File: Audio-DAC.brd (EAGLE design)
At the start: 99 x 99 mm, 201 parts, among them CON1 USB-5075BR-04-WH, CON2 VOL_CON, CON3 SWD_CON, IC1 3.3V 200mA, IC10 15V, IC11 -15V, IC12 3.3V, IC13 LPC1114FDH28, IC14 10V, IC15 5V, IC16 5V, IC17 3.3V, IC18 TC7WH74FU, IC19 AK4495EQ, IC2 AT32UC3A3256, IC20 TC7WU04FU, IC21 10V, IC22 -10V, IC23 OP275, IC3 SI8420, IC4 SI8420, IC5 SI8420, IC6 SI8420, IC9 7805, Q1 NPN2SC3422, Q2 PNP2SA1359, Q3 NPN2SC3422, Q4 PNP2SA1359, Q5 NPN2SC3325, Q6 NPN2SC3325, SW1 EA2, SW2 EA2, X1 12MHz, X2 24.576MHz, X3 22.5792MHz

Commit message: 発注
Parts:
- removed JP1: SPK, pinhead:1X04
- removed JP2: HP, pinhead:1X04
- added R15: 100, my_rcl:1608-J
- added R16: DNP, my_rcl:1608-J
- added TP25: GND, my_connector:TESTPIN
- added TP26: +3V3D, my_connector:TESTPIN
- added TP27, TP31: GND_L, my_connector:TESTPIN-BIG
- added TP28: SPK_L, my_connector:TESTPIN-BIG
- added TP29: SPK_R, my_connector:TESTPIN-BIG
- added TP30, TP34: GND_R, my_connector:TESTPIN-BIG
- added TP32: HP_L, my_connector:TESTPIN-BIG
- added TP33: HP_R, my_connector:TESTPIN-BIG
- C47, C48, C52, C54: value 0.22u -> 0.1u
- C49, C50, C55, C56: value DNP -> 0.1u
- C63, C64, C65, C66: value 2000p -> 10n
- CON1: value USB-5075BR-04-WH -> USB-B
- CON2: value VOL_CON -> VOLUEME
- CON3: value SWD_CON -> SWD
- D7, D8: value SBD-1A -> SBD; device my_rcl:TUMD2M -> my_rcl:SOD123
- FB1, FB2, FB3, FB4: value FB-1608 -> FB; device my_rcl:1608 -> my_rcl:1608-J
- IC1: value 3.3V 200mA -> 3.3V
- IC10: value 15V -> +15V
- IC13: value LPC1114FDH28 -> LPC1114
- IC14, IC21: value 10V -> +10V
- IC15, IC16: value 5V -> +5V
- IC17: value 3.3V -> +3.3V
- Q5, Q6: value NPN2SC3325 -> NPN
- R32, R33, R34, R35, R36: device my_rcl:1608 -> my_rcl:1608-J
- R37, R38, R39, R40: value 1k -> 2k
- R41, R42, R43, R44: value 2k -> 4k
- R45, R46, R47, R48: value 1k -> 150
- TP10: value TEST_11 -> GND
- TP11: value TEST_10 -> SDA
- TP13: value GND -> TEST_10
- TP14: value +3V3 -> TEST_14
- TP15, TP18: value SP_SW -> SP
- TP16: value HP_SW -> HP
- TP17: value GND -> +12V
- TP19: value HP_SW -> GND
- TP20: value +12V -> HP
- TP23: value SDA -> TEST_11
- TP5: value VIN+ -> V+
- TP8: value VIN- -> V-
- TP9: value TEST_12 -> +3V3
- moved TP17 69.6 mm to (91.4, 91.4)
- moved TP21 69.0 mm to (36.8, 48.3)
- moved TP23 8.03 mm to (45.7, 26.7)
- moved TP6 7.62 mm to (73.7, 5.08)
- moved TP20 7.41 mm to (94.0, 88.9)
- moved DR3 6.35 mm to (89.5, 3.17)
- moved DR4 6.35 mm to (89.5, 95.9)
- moved TP11 5.68 mm to (38.1, 29.2)
- moved TP14 5.08 mm to (45.7, 24.1)
- moved TP9 5.08 mm to (45.7, 29.2)
- moved TP7 5.08 mm to (78.7, 5.08)
- moved FB2 4.05 mm to (9.84, 55.2), turned to 0 degrees
- moved TP10 3.59 mm to (43.2, 29.2)
- moved DR2 3.17 mm to (6.35, 95.9)
- moved D8 2.73 mm to (93.0, 77.8)
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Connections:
- removed net N$37: IC13.14, TP9.1
- removed net N$53: IC13.10, TP11.1
- new net N$15: C1.1, IC1.4
- new net N$16: D7.1, Q5.3, SW1.1
- new net N$19: IC13.14, TP14.1
- net +12V: now also D7.2, D8.2, SW1.10, TP17.1; no longer D7.K, D8.K, SW1.1, TP20.1
- net +3V3: now also TP9.1; no longer TP14.1
- net +3V3D: now also IC1.5, TP26.1; no longer IC1.4
- net DAC_DVDD: now also IC19.44; no longer IC19.43
- net DAC_LRCLK: now also R15.1
- net DGND: now also TP25.1
- net EN_+3V3D: now also IC1.3, R16.1; no longer IC1.1
- net GND: now also IC19.43, IC9.2, TP10.1, TP19.1, TP27.1, TP30.1, TP31.1, TP34.1; no longer IC19.44, IC9.3, JP1.1, JP1.4, JP2.1, JP2.4, TP13.1, TP17.1
- net HP_L: now also TP32.1; no longer JP2.2
- net HP_R: now also TP33.1; no longer JP2.3
- net HP_SW: now also TP20.1; no longer TP19.1
- net I2C_SDA: now also TP11.1; no longer TP23.1
- net N$18: now also IC13.10, TP13.1; no longer C1.1, IC1.3
- net N$36: now also IC13.11, TP23.1; no longer D7.A, Q5.3, SW1.10
- net N$38: now also IC13.2, R15.2; no longer IC13.11, TP10.1
- net N$49: now also D8.1; no longer D8.A
- net N$51: now also IC9.3; no longer IC9.2
- net SPK_L: now also TP28.1; no longer JP1.2
- net SPK_R: now also TP29.1; no longer JP1.3
- net USB_VBUS: now also IC1.1, R16.2; no longer IC1.5
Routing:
- net N$19: track 0.00 -> 20.0 mm, vias 0 -> 1
- net N$37: track 19.3 -> 0.00 mm, vias 1 -> 0
- net N$53: track 16.5 -> 0.00 mm
- net N$16: track 0.00 -> 15.7 mm
- net N$18: track 1.76 -> 16.9 mm
- net N$38: track 17.2 -> 10.2 mm
- net GND: track 138.2 -> 145.2 mm
- net V-: track 117.4 -> 110.6 mm, vias 5 -> 3
- net N$49: track 14.5 -> 9.35 mm
- net N$36: track 21.3 -> 17.9 mm
- net N$10: track 6.36 -> 3.42 mm
- net USB_VBUS: track 35.1 -> 38.0 mm
- net +3V3: track 110.3 -> 112.6 mm
- net DAC_DVDD: track 7.88 -> 5.68 mm
- net V+: track 148.1 -> 146.2 mm
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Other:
- board size 99 x 99 mm -> 97 x 99 mm
- board text added: "Audio DAC v6.1"
- board text removed: "Audio DAC v6"

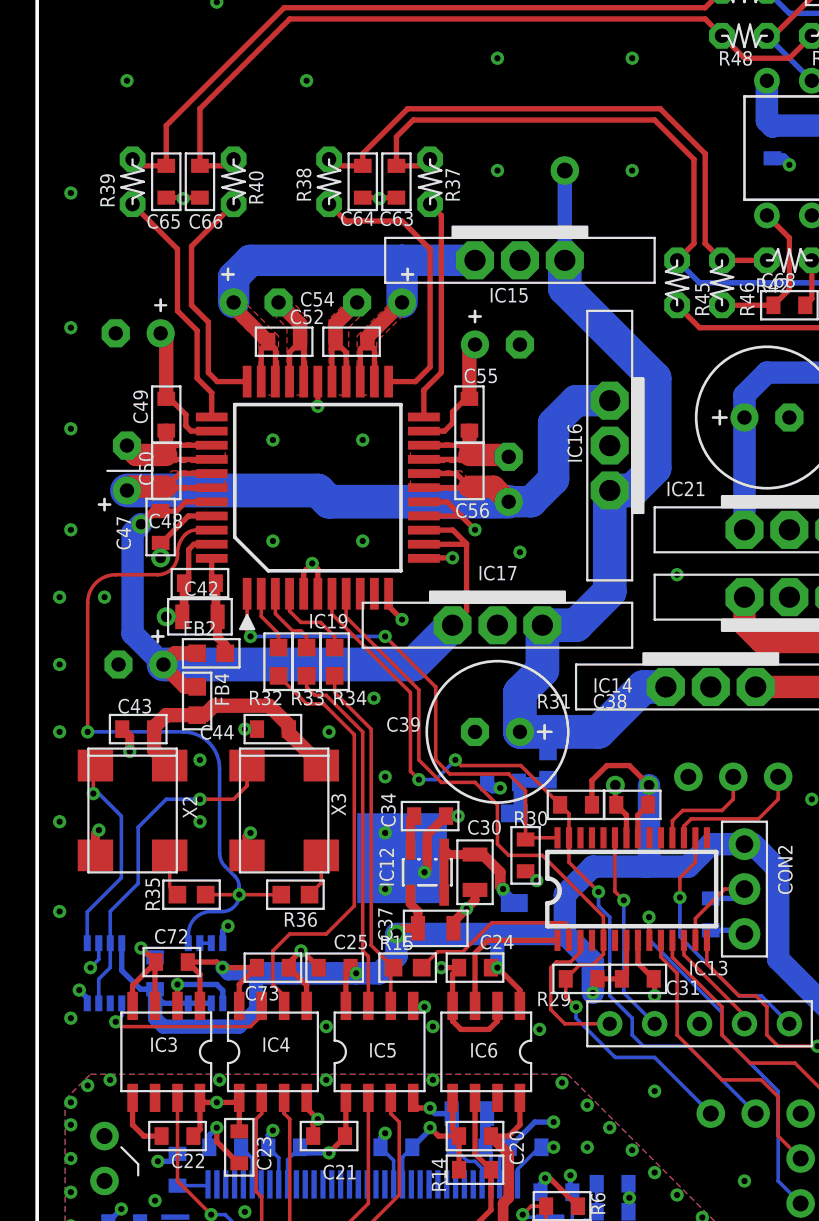
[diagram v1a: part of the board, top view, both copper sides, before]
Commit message: Change to AK4493
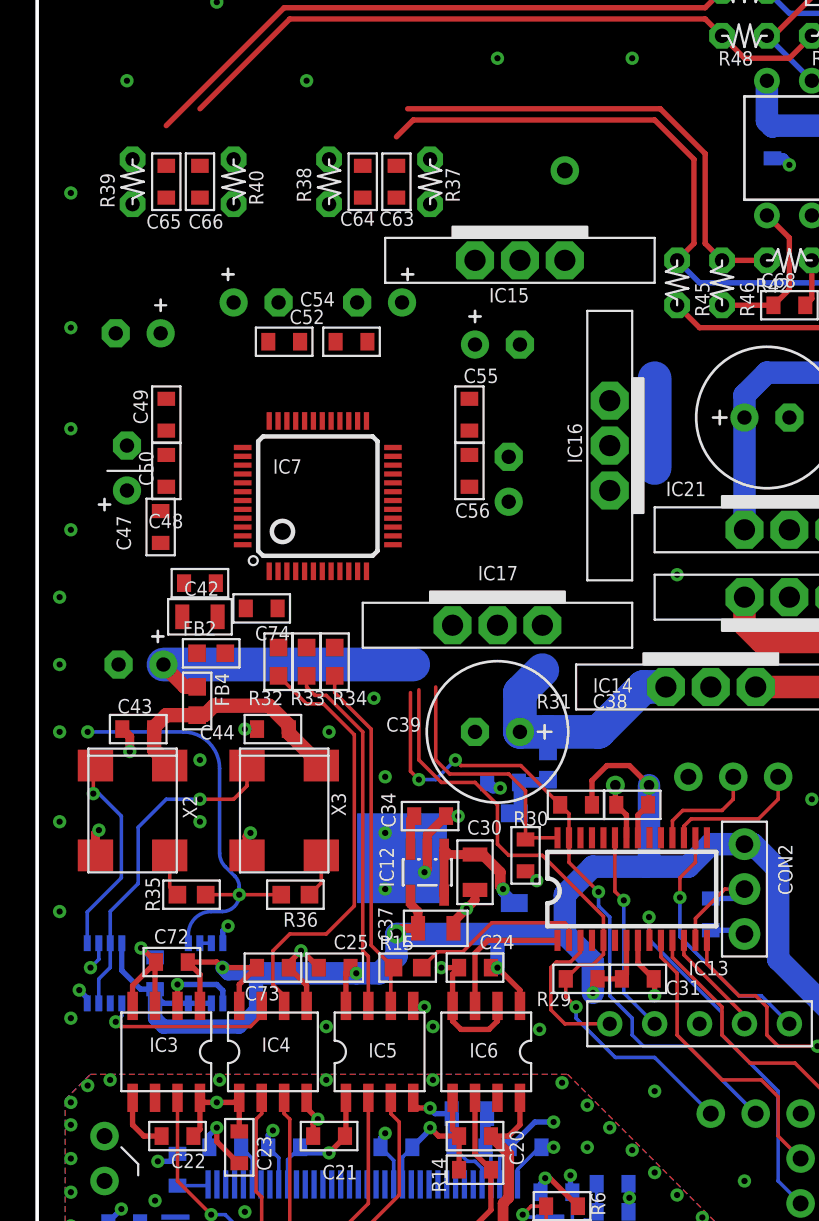
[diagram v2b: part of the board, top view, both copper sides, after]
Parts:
- removed IC19: AK4495EQ, my_ic:LQFP44
- added C74: 1u, my_rcl:1608
- added IC7: AK4493EQ, my_ic:LQFP48
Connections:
- new net N$37: C74.1, IC7.1
- net DAC_AVDD: now also IC7.14, IC7.15, IC7.16, IC7.44; no longer IC19.13, IC19.14, IC19.40
- net DAC_DVDD: now also IC7.48; no longer IC19.44
- net DAC_LN: now also IC7.35; no longer IC19.33
- net DAC_LP: now also IC7.36; no longer IC19.34
- net DAC_MCLK: now also IC7.46; no longer IC19.42
- net DAC_PDN: now also IC7.2; no longer IC19.1
- net DAC_RN: now also IC7.26; no longer IC19.23
- net DAC_RP: now also IC7.25; no longer IC19.22
- net DAC_VCC: now also IC7.27, IC7.28, IC7.33, IC7.34; no longer IC19.24, IC19.25, IC19.31, IC19.32
- net DAC_VREF: now also IC7.19, IC7.20, IC7.41, IC7.42; no longer IC19.17, IC19.18, IC19.38, IC19.39
- net GND: now also C74.2, IC7.12, IC7.13, IC7.17, IC7.18, IC7.21, IC7.22, IC7.29, IC7.30, IC7.31, IC7.32, IC7.39, IC7.40, IC7.45, IC7.47, IC7.6, IC7.7; no longer IC19.11, IC19.12, IC19.15, IC19.16, IC19.19, IC19.20, IC19.26, IC19.27, IC19.28, IC19.29, IC19.30, IC19.36, IC19.37, IC19.41, IC19.43, IC19.5, IC19.6
- net I2C_SCL: now also IC7.8; no longer IC19.7
- net I2C_SDA: now also IC7.9; no longer IC19.8
- net N$41: now also IC7.3; no longer IC19.2
- net N$42: now also IC7.5; no longer IC19.4
- net N$43: now also IC7.4; no longer IC19.3
- net VCOM_L: now also IC7.38; no longer IC19.35
- net VCOM_R: now also IC7.23; no longer IC19.21
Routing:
- net GND: track 145.2 -> 82.9 mm, vias 95 -> 78
- net DAC_VREF: track 47.6 -> 0.00 mm
- net DAC_VCC: track 33.6 -> 0.00 mm
- net +12V: track 87.1 -> 57.3 mm
- net DAC_AVDD: track 45.4 -> 16.6 mm, vias 1 -> 0
- net DAC_MCLK: track 40.7 -> 24.4 mm
- net DAC_RN: track 16.1 -> 0.00 mm
- net DAC_PDN: track 28.7 -> 14.5 mm, vias 2 -> 0
- net DAC_LP: track 13.9 -> 0.00 mm
- net DAC_LN: track 13.3 -> 0.00 mm
- net DAC_RP: track 12.7 -> 0.00 mm
- net VCOM_L: track 7.54 -> 0.00 mm
- net I2C_SCL: track 45.6 -> 38.2 mm
- net I2C_SDA: track 43.7 -> 36.5 mm
- net VCOM_R: track 6.90 -> 0.00 mm
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- removed copper zone on layer 1, net DAC_VCC
- removed copper zone on layer 1, net DAC_VREF
- removed copper zone on layer 1, net GND

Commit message: 大体できた
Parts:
- removed C71: 10u, my_rcl:2012
- removed TP21: GND, my_connector:TESTPIN
- removed TP22: +12V, my_connector:TESTPIN
- TP15: value SP -> +12V
- TP16: value HP -> +12V
- TP17: value +12V -> SW_SP
- TP18: value SP -> SW_HP
- TP19: value GND -> SW_HP
- TP20: value HP -> SW_SP
- moved R59 69.0 mm to (36.8, 47.6), turned to 270 degrees
- moved R60 66.4 mm to (38.7, 47.6), turned to 90 degrees
- moved R57 66.3 mm to (36.8, 47.6), flipped to the bottom, turned to 270 degrees
- moved R58 64.8 mm to (38.7, 47.6), flipped to the bottom
- moved TP20 64.3 mm to (46.4, 45.7)
- moved TP18 60.8 mm to (46.4, 48.3)
- moved Q6 60.6 mm to (43.5, 48.3), turned to 0 degrees
- moved Q5 60.2 mm to (41.9, 47.6), flipped to the bottom, turned to 90 degrees
- moved D8 59.7 mm to (40.6, 49.2), turned to 90 degrees
- moved D7 58.3 mm to (39.7, 50.8), flipped to the bottom
- moved TP16 42.3 mm to (76.2, 73.0)
- moved Q4 29.0 mm to (88.9, 91.8), turned to 0 degrees
- moved Q3 29.0 mm to (78.7, 91.8), turned to 0 degrees
- moved D5 27.2 mm to (80.0, 88.6), turned to 180 degrees
- moved D6 27.2 mm to (90.2, 88.6), turned to 0 degrees
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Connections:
- removed net HP_SW: IC13.17, R59.2, TP16.1, TP20.1
- removed net N$16: D7.1, Q5.3, SW1.1
- removed net N$49: D8.1, Q6.3, SW2.1
- removed net SP_SW: IC13.18, R57.2, TP15.1, TP18.1
- new net EN_HP: IC13.17, R59.2
- new net EN_SP: IC13.18, R57.2
- new net SW_HP: D8.1, Q6.3, SW2.1, TP18.1, TP19.1
- new net SW_SP: D7.1, Q5.3, SW1.1, TP17.1, TP20.1
- net +12V: now also TP15.1, TP16.1; no longer C71.1, TP17.1, TP22.1
- net GND: no longer C71.2, TP19.1, TP21.1
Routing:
- net DAC_VREF: track 0.00 -> 51.3 mm
- net DAC_VCC: track 0.00 -> 36.8 mm
- net DAC_AVDD: track 16.6 -> 51.4 mm
- net GND: track 82.9 -> 115.8 mm, vias 78 -> 70
- net V-: track 110.6 -> 142.1 mm, vias 3 -> 0
- net +12V: track 57.3 -> 85.7 mm, vias 1 -> 0
- net N$27: track 24.7 -> 52.0 mm, vias 0 -> 1
- net DAC_RN: track 0.00 -> 20.4 mm
- net N$46: track 35.5 -> 16.4 mm
- net DAC_LP: track 0.00 -> 18.4 mm
- net DAC_RP: track 0.00 -> 17.3 mm
- net DAC_LN: track 0.00 -> 17.1 mm
- net N$47: track 26.8 -> 11.1 mm
- net N$16: track 15.7 -> 0.00 mm
- net DAC_MCLK: track 24.4 -> 39.2 mm
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- removed copper zone on layer 16, net GND
- removed copper zone on layer 1, net V+
- removed copper zone on layer 1, net V-
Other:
- board text added: "Audio DAC v7"
- board text removed: "Audio DAC v6.1"

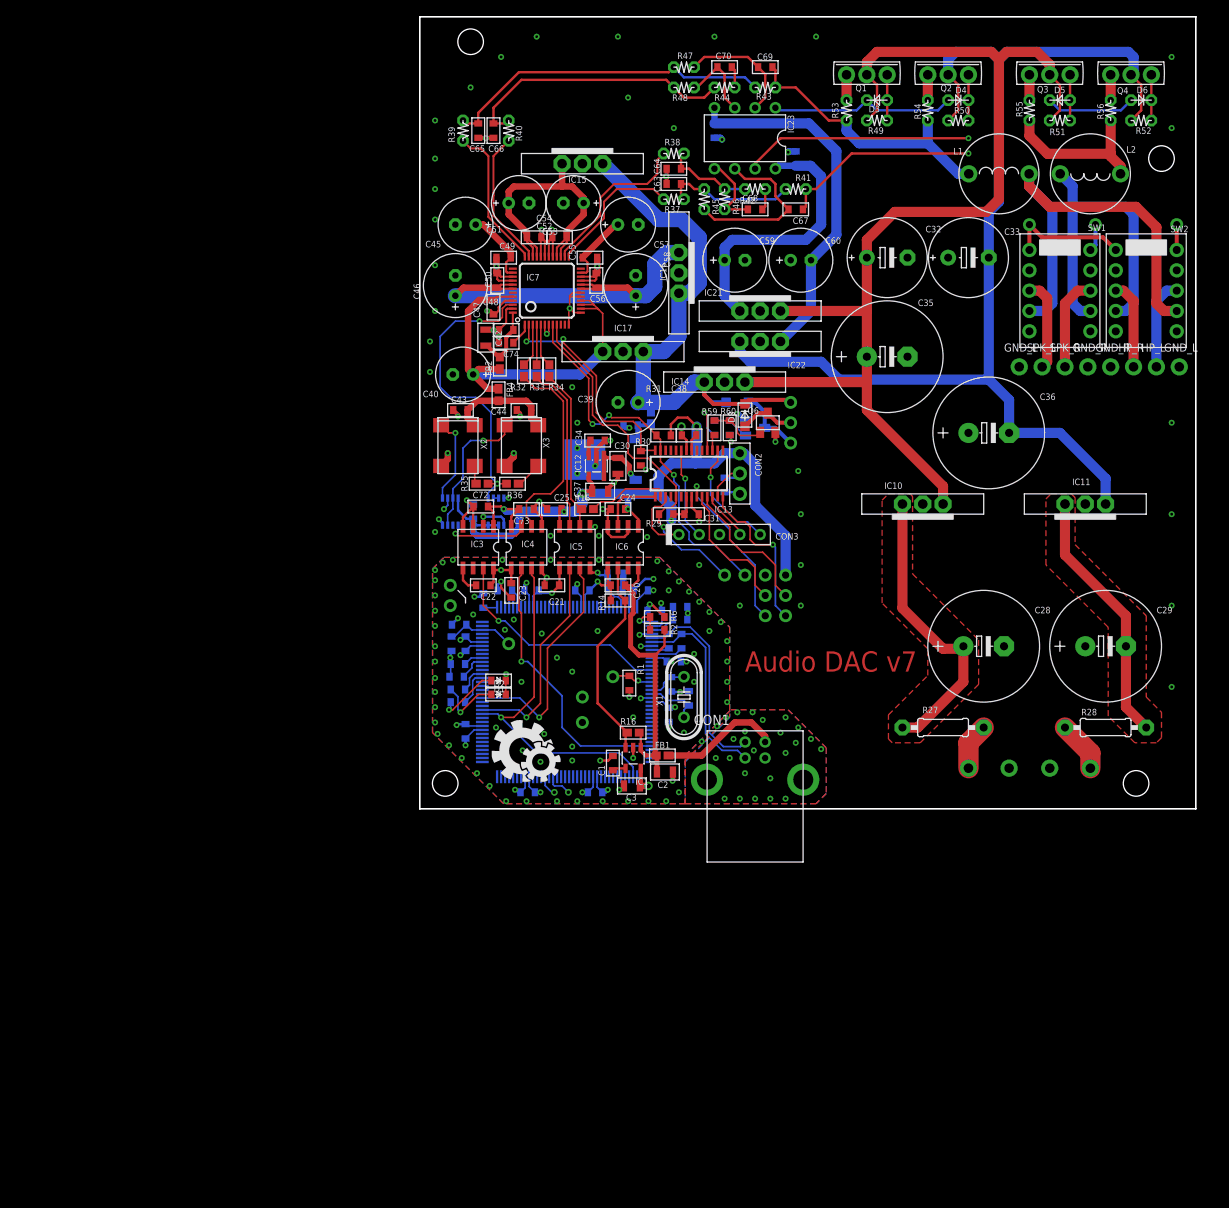
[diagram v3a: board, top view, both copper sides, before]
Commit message: シルク調整
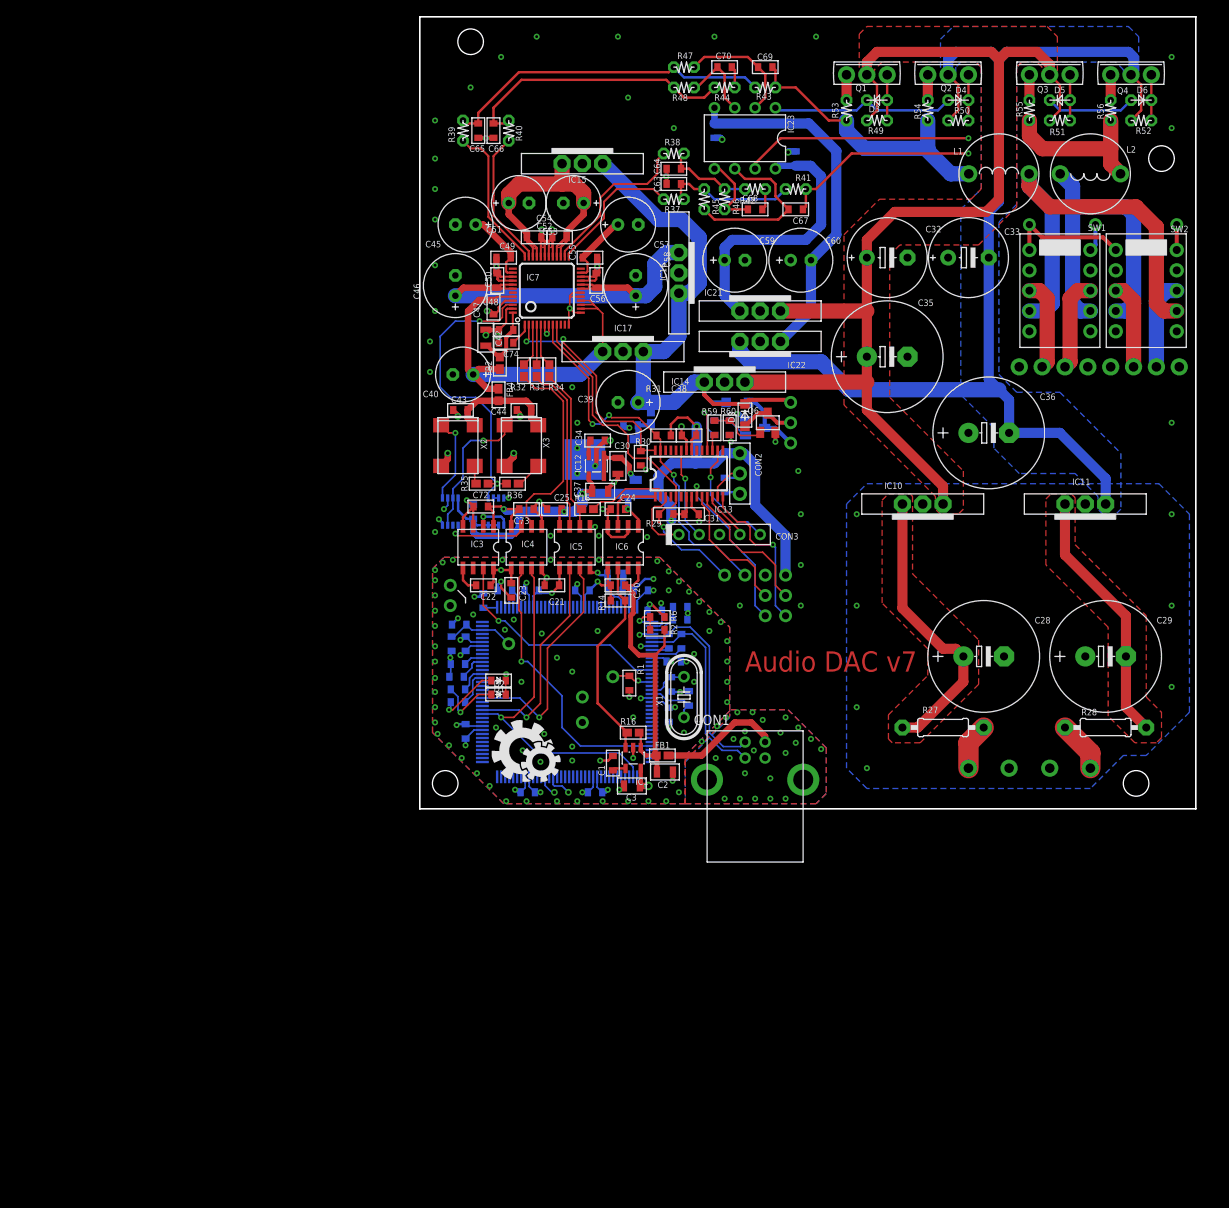
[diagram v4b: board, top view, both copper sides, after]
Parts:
- moved C28 1.27 mm to (70.5, 19.1)
- moved C29 1.27 mm to (85.7, 19.1)
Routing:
- net N$33: track 41.2 -> 50.9 mm
- net V-: track 142.1 -> 143.9 mm
- net GND: track 115.8 -> 116.9 mm, vias 70 -> 74
- net VIN+: track 37.3 -> 36.3 mm
- net N$32: track 34.9 -> 35.9 mm
- added copper zone on layer 1, net DAC_VCC
- added copper zone on layer 1, net DAC_VREF
- added copper zone on layer 1, net GND
- added copper zone on layer 16, net GND
- added copper zone on layer 1, net V+
- added copper zone on layer 16, net V-

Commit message: 発注
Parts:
- moved C65 0.63 mm to (7.30, 84.1)
- moved C66 0.63 mm to (9.21, 84.1)
- moved R39 0.63 mm to (5.40, 84.1)
- moved R40 0.63 mm to (11.1, 84.1)
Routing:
- net GND: track 116.9 -> 114.6 mm, vias 74 -> 91
- net +12V: track 85.7 -> 87.4 mm
- net N$45: track 34.5 -> 35.2 mm
- net N$44: track 41.4 -> 42.0 mm
- net DAC_LP: track 18.4 -> 17.8 mm
- net DAC_LN: track 17.1 -> 16.5 mm
